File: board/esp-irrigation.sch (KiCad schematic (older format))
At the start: 23 parts, among them J1 ESP01_Header, J2 AC IN, J3 Valves, U1 MCP23008-xSO, U2 SMDA36-7, U3 LM2594HVM-3.3

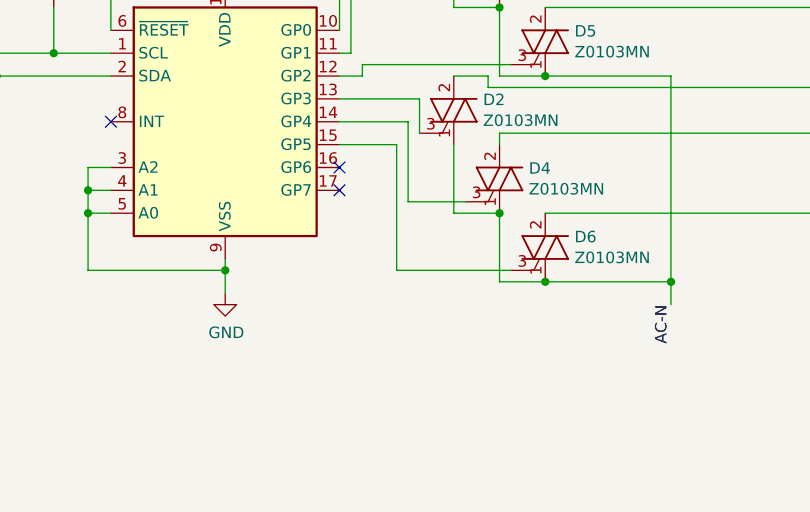
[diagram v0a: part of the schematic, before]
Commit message: add indicator leds
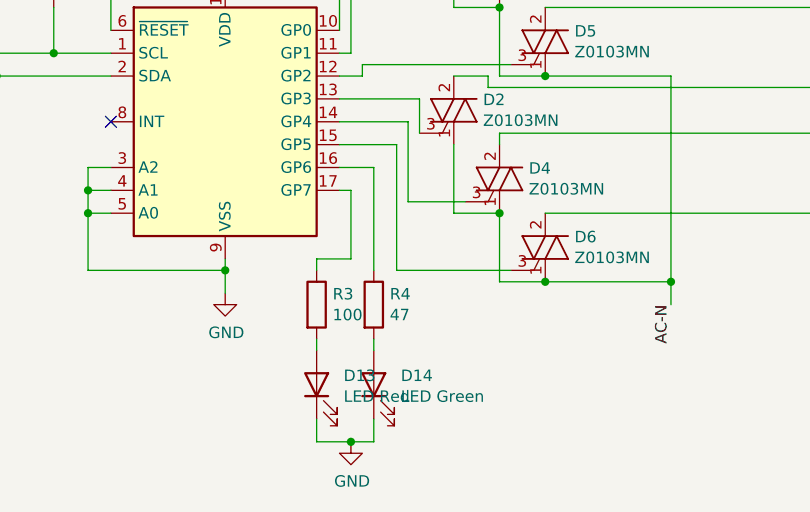
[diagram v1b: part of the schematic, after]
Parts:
- added D13: LED Red, LED_THT:LED_D3.0mm, symbol Device:LED
- added D14: LED Green, LED_THT:LED_D3.0mm, symbol Device:LED
- added R3: 100, Resistor_SMD:R_0805_2012Metric_Pad1.20x1.40mm_HandSolder, symbol Device:R
- added R4: 47, Resistor_SMD:R_0805_2012Metric_Pad1.20x1.40mm_HandSolder, symbol Device:R
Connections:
- net GND: now also D13.1 (K), D14.1 (K)
- net at U1.16 (GP6): now also R4.1
- net at U1.17 (GP7): now also R3.1
- new net: D13.2 (A), R3.2
- new net: D14.2 (A), R4.2
- no-connect marks 10 -> 8
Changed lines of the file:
@@
 NoConn ~ 1250 2350
 NoConn ~ 1750 2450
-NoConn ~ 2750 5000
-NoConn ~ 2750 4900
 NoConn ~ 1750 4700
+$Comp
+L Device:R R3
+U 1 1 62B78E00
+P 2650 5500
+F 0 "R3" H 2720 5546 50  0000 L CNN
+F 1 "100" H 2720 5455 50  0000 L CNN
+F 2 "Resistor_SMD:R_0805_2012Metric_Pad1.20x1.40mm_HandSolder" V 2580 5500 50  0001 C CNN
+F 3 "~" H 2650 5500 50  0001 C CNN
+	1    2650 5500
+	1    0    0    -1
+$EndComp
+$Comp
+L Device:R R4
+U 1 1 62B798E0
+P 2900 5500
+F 0 "R4" H 2970 5546 50  0000 L CNN
+F 1 "47" H 2970 5455 50  0000 L CNN
+F 2 "Resistor_SMD:R_0805_2012Metric_Pad1.20x1.40mm_HandSolder" V 2830 5500 50  0001 C CNN
+F 3 "~" H 2900 5500 50  0001 C CNN
+	1    2900 5500
+	1    0    0    -1
+$EndComp
+Wire Wire Line
+	2750 4900 2900 4900
+Wire Wire Line
+	2750 5000 2800 5000
+Wire Wire Line
+	2800 5000 2800 5300
+Wire Wire Line
+	2800 5300 2650 5300
+Wire Wire Line
+	2650 5300 2650 5350
+Wire Wire Line
+	2650 5650 2650 5700
+Wire Wire Line
+	2900 4900 2900 5350
+$Comp
+L Device:LED D14
+U 1 1 62BB4D6E
+P 2900 5850
+F 0 "D14" V 2939 5732 50  0000 R CNN
+F 1 "LED Green" V 2848 5732 50  0000 R CNN
+F 2 "LED_THT:LED_D3.0mm" H 2900 5850 50  0001 C CNN
+F 3 "~" H 2900 5850 50  0001 C CNN
+	1    2900 5850
+	0    -1   -1   0
+$EndComp
+Wire Wire Line
+	2900 5650 2900 5700
+$Comp
+L power:GND #PWR0101
+U 1 1 62BBBD63
+P 2800 6100
+F 0 "#PWR0101" H 2800 5850 50  0001 C CNN
+F 1 "GND" H 2805 5927 50  0000 C CNN
+F 2 "" H 2800 6100 50  0001 C CNN
+F 3 "" H 2800 6100 50  0001 C CNN
+	1    2800 6100
+	1    0    0    -1
+$EndComp
+Wire Wire Line
+	2650 6000 2650 6100
+Wire Wire Line
+	2650 6100 2800 6100
+Wire Wire Line
+	2900 6000 2900 6100
+Wire Wire Line
+	2900 6100 2800 6100
+Connection ~ 2800 6100
+$Comp
+L Device:LED D13
+U 1 1 62B873C5
+P 2650 5850
+F 0 "D13" V 2689 5732 50  0000 R CNN
+F 1 "LED Red" V 2598 5732 50  0000 R CNN
+F 2 "LED_THT:LED_D3.0mm" H 2650 5850 50  0001 C CNN
+F 3 "~" H 2650 5850 50  0001 C CNN
+	1    2650 5850
+	0    -1   -1   0
+$EndComp
 $EndSCHEMATC
